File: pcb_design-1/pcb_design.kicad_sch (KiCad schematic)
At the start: 4 parts, among them SW1 SW_Push, SW2 SW_Push, SW3 SW_Push, U1 MOUDLE-SEEEDUINO-XIAO

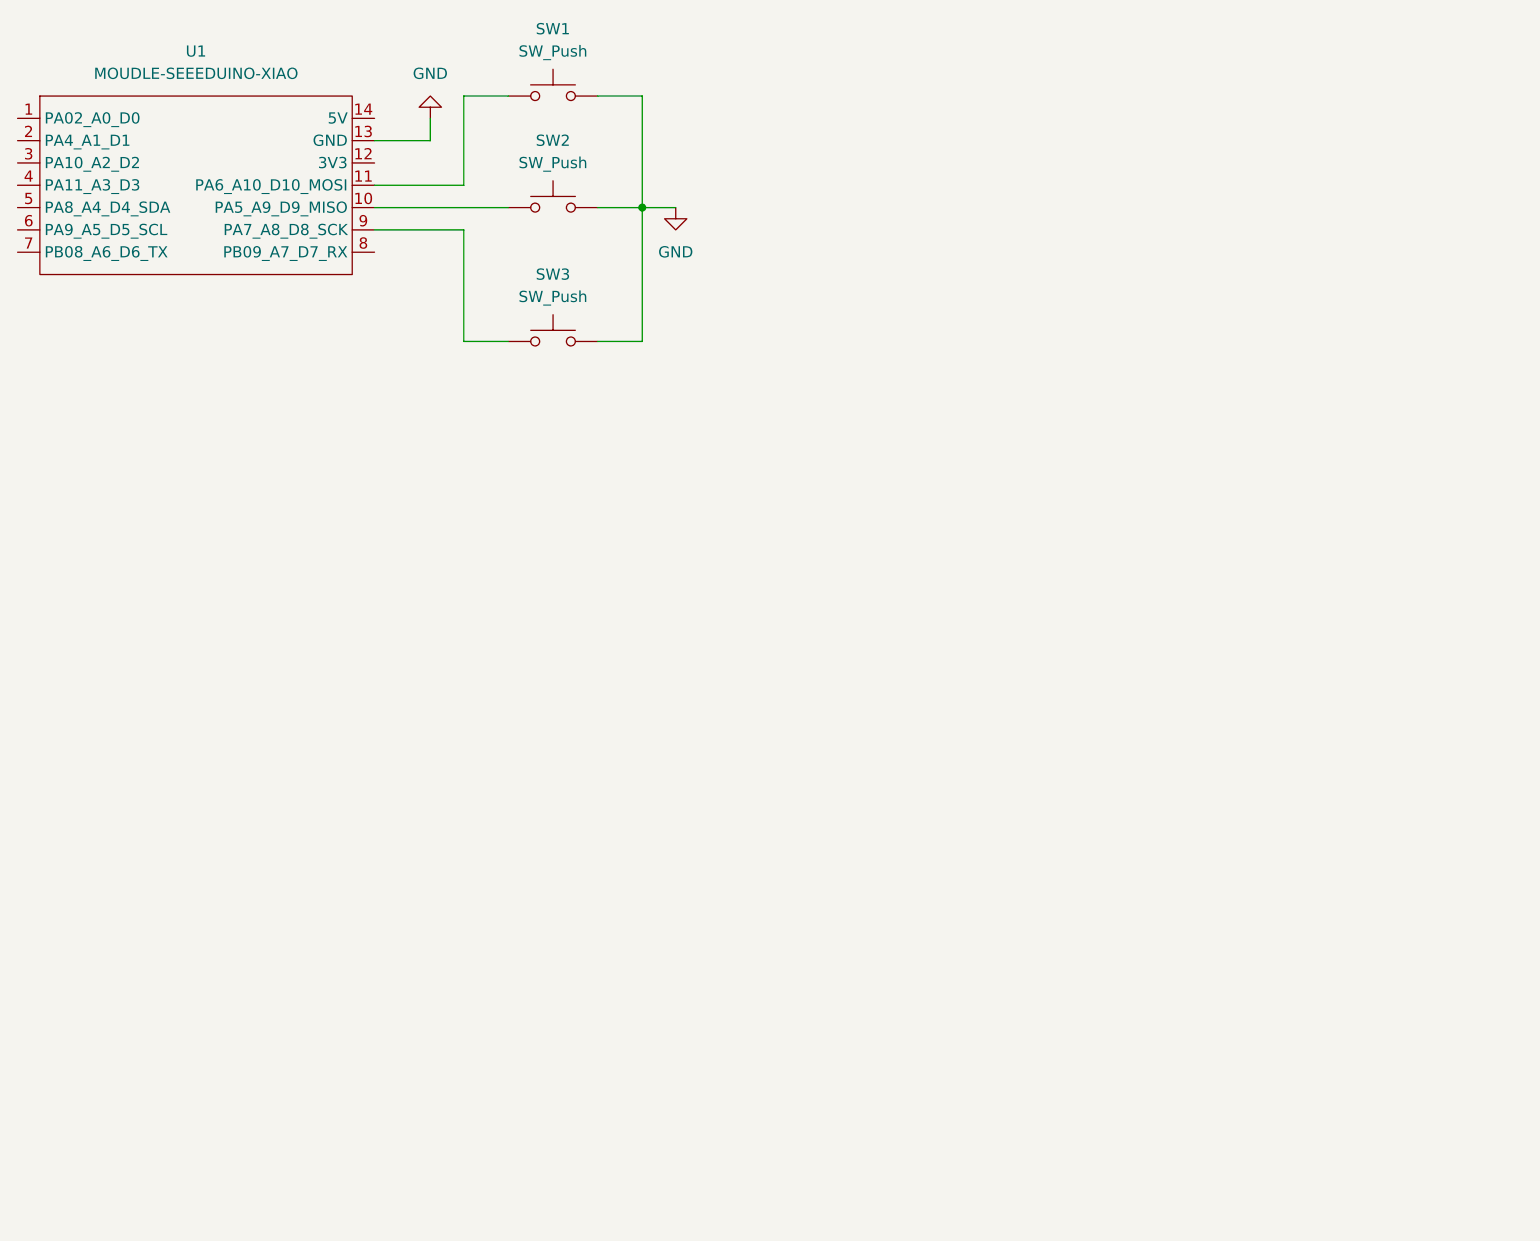
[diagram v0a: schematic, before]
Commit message: Polish codebase: complete macro pad firmware, update KiCad project files, and add detailed README documentation with schematic/PCB renders
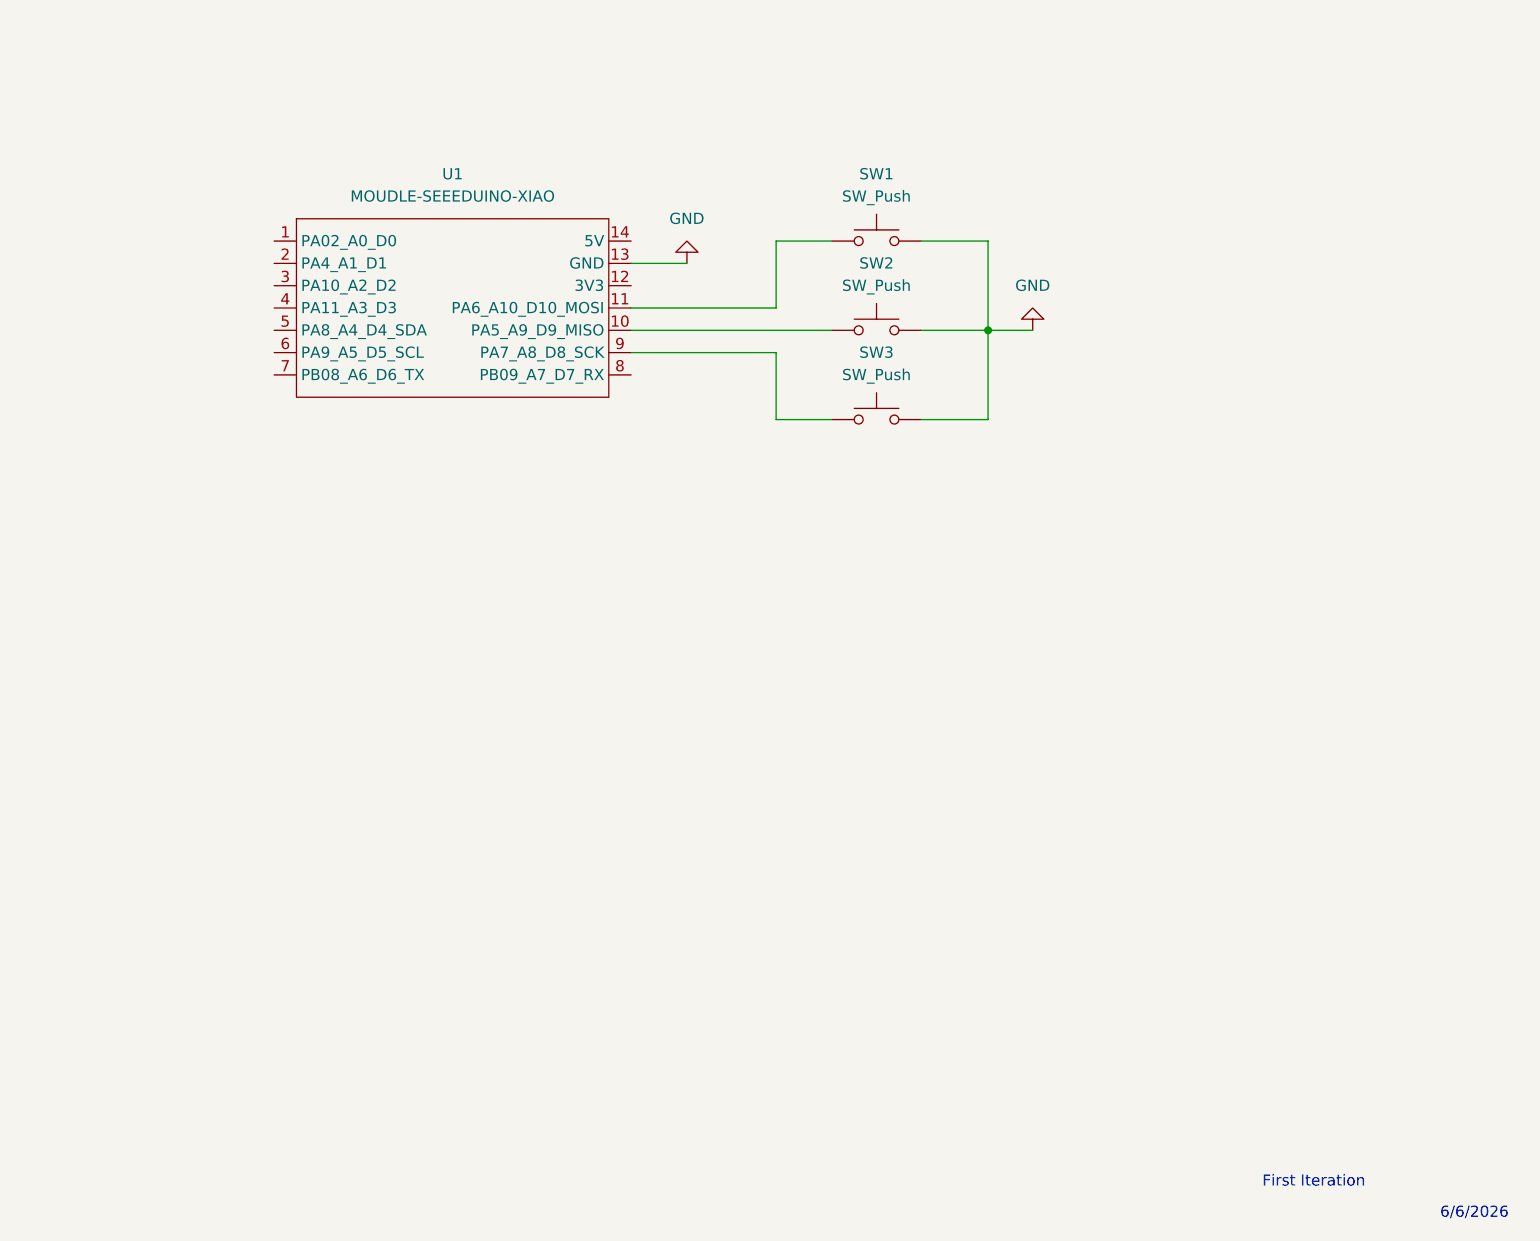
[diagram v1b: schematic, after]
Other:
- note added: "6/6/2026"
- note added: "First Iteration"
